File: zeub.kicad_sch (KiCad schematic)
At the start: 25 parts, among them J1 debug-port, J2 OLED-128x32, J5 Conn_01x03, J6 Conn_01x03, Q1 AO3401A, Q2 AO3401A, Q3 AO3401A, Q4 AO3401A, Q5 AO3401A, SW1 SKRHA, SW2 RotaryEncoder_Switch, U5 holyiot-18010-no-underside, U6 MT25QL128ABA1ESE

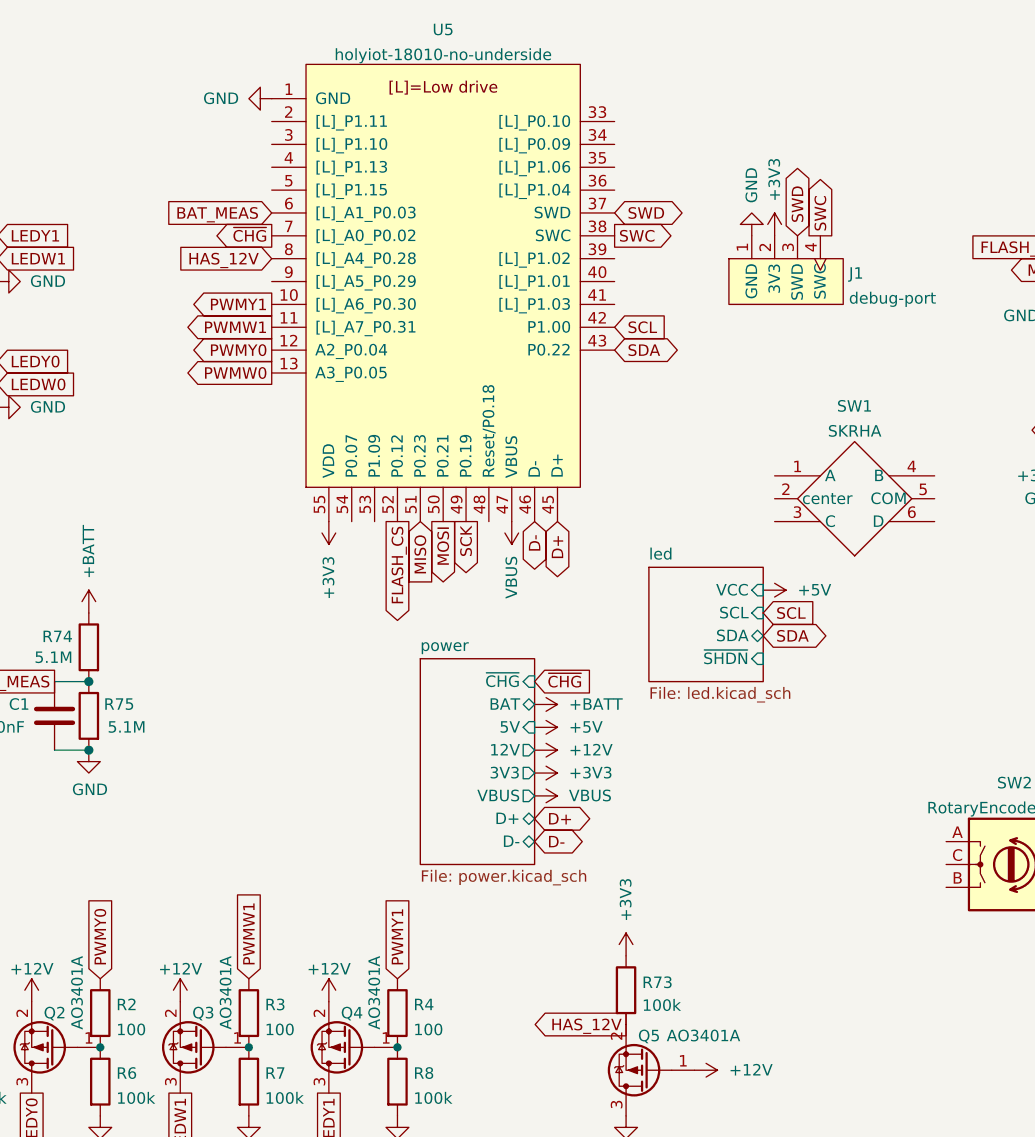
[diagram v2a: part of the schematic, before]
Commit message: routed PMU + rull RGB
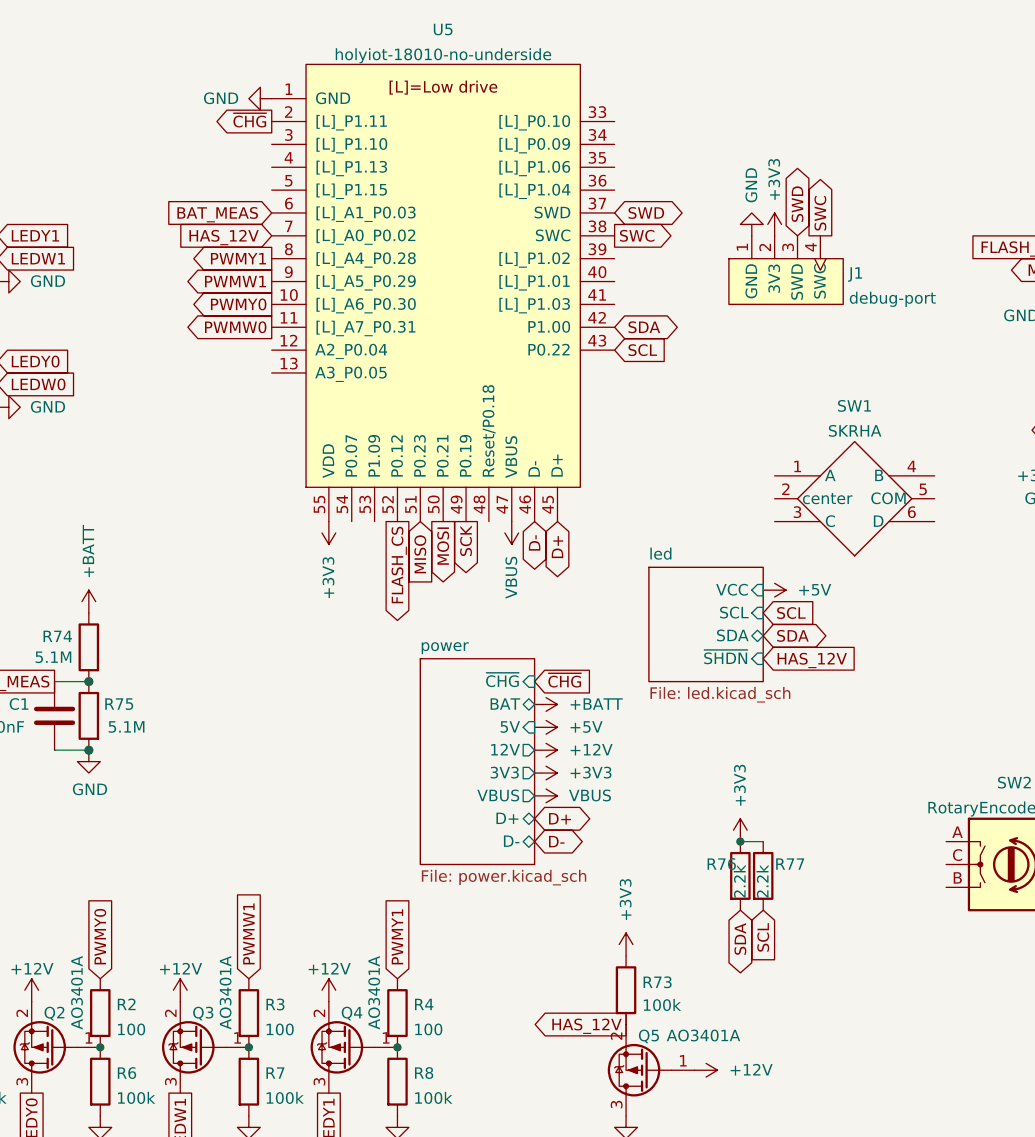
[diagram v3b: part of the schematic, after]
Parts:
- added R76, R77: 2.2k, Resistor_SMD:R_0603_1608Metric, symbol Device:R
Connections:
- net +3V3: now also R76.1, R77.1
- net HAS_12V: now also U5.7 ([L]_A0_P0.02); no longer U5.8 ([L]_A4_P0.28)
- net PWMW0: now also U5.11 ([L]_A7_P0.31); no longer U5.13 (A3_P0.05)
- net PWMW1: now also U5.9 ([L]_A5_P0.29); no longer U5.11 ([L]_A7_P0.31)
- net PWMY0: now also U5.10 ([L]_A6_P0.30); no longer U5.12 (A2_P0.04)
- net PWMY1: now also U5.8 ([L]_A4_P0.28); no longer U5.10 ([L]_A6_P0.30)
- net SCL: now also U5.43 (P0.22), R77.2; no longer U5.42 (P1.00)
- net SDA: now also U5.42 (P1.00), R76.2; no longer U5.43 (P0.22)
- net ~{CHG}: now also U5.2 ([L]_P1.11); no longer U5.7 ([L]_A0_P0.02)
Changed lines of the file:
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@@
   (junction (at 24.13 134.62) (diameter 0) (color 0 0 0 0)
+  )
+  (junction (at 111.76 111.76) (diameter 0) (color 0 0 0 0)
   )
   (junction (at 73.66 134.62) (diameter 0) (color 0 0 0 0)
@@
   (wire (pts (xy 35.56 93.98) (xy 39.37 93.98))
     (stroke (width 0) (type solid) (color 0 0 0 0))
+  )
+  (wire (pts (xy 111.76 111.76) (xy 114.3 111.76))
+    (stroke (width 0) (type default) (color 0 0 0 0))
   )
   (wire (pts (xy 39.37 101.6) (xy 35.56 101.6))
@@
     )
   )
+  (global_label "HAS_12V" (shape input) (at 114.3 91.44 0) (fields_autoplaced)
+    (effects (font (size 1.27 1.27)) (justify left))
+    (property "Intersheet References" "${INTERSHEET_REFS}" (id 0) (at 124.8169 91.5194 0)
+      (effects (font (size 1.27 1.27)) (justify left) hide)
+    )
+  )
   (global_label "SDA" (shape bidirectional) (at 114.3 88.9 0) (fields_autoplaced)
     (effects (font (size 1.27 1.27)) (justify left))
@@
     )
   )
-  (global_label "PWMW1" (shape output) (at 59.69 54.61 180) (fields_autoplaced)
+  (global_label "PWMW1" (shape output) (at 59.69 49.53 180) (fields_autoplaced)
     (effects (font (size 1.27 1.27)) (justify right))
-    (property "Intersheet References" "${INTERSHEET_REFS}" (id 0) (at 50.4431 54.6894 0)
+    (property "Intersheet References" "${INTERSHEET_REFS}" (id 0) (at 50.4431 49.6094 0)
       (effects (font (size 1.27 1.27)) (justify right) hide)
     )
@@
     )
   )
-  (global_label "PWMY1" (shape output) (at 59.69 52.07 180) (fields_autoplaced)
+  (global_label "PWMY1" (shape output) (at 59.69 46.99 180) (fields_autoplaced)
     (effects (font (size 1.27 1.27)) (justify right))
-    (property "Intersheet References" "${INTERSHEET_REFS}" (id 0) (at 50.8059 52.1494 0)
+    (property "Intersheet References" "${INTERSHEET_REFS}" (id 0) (at 50.8059 47.0694 0)
       (effects (font (size 1.27 1.27)) (justify right) hide)
     )
   )
-  (global_label "SDA" (shape bidirectional) (at 97.79 57.15 0) (fields_autoplaced)
+  (global_label "SDA" (shape bidirectional) (at 97.79 54.61 0) (fields_autoplaced)
     (effects (font (size 1.27 1.27)) (justify left))
-    (property "Intersheet References" "${INTERSHEET_REFS}" (id 0) (at 103.7712 57.0706 0)
+    (property "Intersheet References" "${INTERSHEET_REFS}" (id 0) (at 103.7712 54.6894 0)
       (effects (font (size 1.27 1.27)) (justify left) hide)
     )
@@
     )
   )
-  (global_label "PWMY0" (shape output) (at 59.69 57.15 180) (fields_autoplaced)
+  (global_label "PWMY0" (shape output) (at 59.69 52.07 180) (fields_autoplaced)
     (effects (font (size 1.27 1.27)) (justify right))
-    (property "Intersheet References" "${INTERSHEET_REFS}" (id 0) (at 50.8059 57.0706 0)
+    (property "Intersheet References" "${INTERSHEET_REFS}" (id 0) (at 50.8059 51.9906 0)
       (effects (font (size 1.27 1.27)) (justify right) hide)
     )
@@
     )
   )
-  (global_label "~{CHG}" (shape output) (at 59.69 44.45 180) (fields_autoplaced)
+  (global_label "~{CHG}" (shape output) (at 59.69 31.75 180) (fields_autoplaced)
     (effects (font (size 1.27 1.27)) (justify right))
-    (property "Intersheet References" "${INTERSHEET_REFS}" (id 0) (at 53.4064 44.3706 0)
+    (property "Intersheet References" "${INTERSHEET_REFS}" (id 0) (at 53.4064 31.6706 0)
       (effects (font (size 1.27 1.27)) (justify right) hide)
     )
@@
     )
   )
-  (global_label "PWMW0" (shape output) (at 59.69 59.69 180) (fields_autoplaced)
+  (global_label "SDA" (shape bidirectional) (at 111.76 119.38 270) (fields_autoplaced)
     (effects (font (size 1.27 1.27)) (justify right))
-    (property "Intersheet References" "${INTERSHEET_REFS}" (id 0) (at 50.4431 59.7694 0)
+    (property "Intersheet References" "${INTERSHEET_REFS}" (id 0) (at 111.8394 125.3612 90)
+      (effects (font (size 1.27 1.27)) (justify right) hide)
+    )
+  )
+  (global_label "PWMW0" (shape output) (at 59.69 54.61 180) (fields_autoplaced)
+    (effects (font (size 1.27 1.27)) (justify right))
+    (property "Intersheet References" "${INTERSHEET_REFS}" (id 0) (at 50.4431 54.6894 0)
       (effects (font (size 1.27 1.27)) (justify right) hide)
     )
@@
     )
   )
-  (global_label "SCL" (shape input) (at 97.79 54.61 0) (fields_autoplaced)
+  (global_label "SCL" (shape input) (at 97.79 57.15 0) (fields_autoplaced)
     (effects (font (size 1.27 1.27)) (justify left))
-    (property "Intersheet References" "${INTERSHEET_REFS}" (id 0) (at 103.7107 54.5306 0)
+    (property "Intersheet References" "${INTERSHEET_REFS}" (id 0) (at 103.7107 57.2294 0)
       (effects (font (size 1.27 1.27)) (justify left) hide)
     )
@@
     )
   )
+  (global_label "SCL" (shape input) (at 114.3 119.38 270) (fields_autoplaced)
+    (effects (font (size 1.27 1.27)) (justify right))
+    (property "Intersheet References" "${INTERSHEET_REFS}" (id 0) (at 114.3794 125.3007 90)
+      (effects (font (size 1.27 1.27)) (justify right) hide)
+    )
+  )
   (global_label "SWD" (shape bidirectional) (at 118.11 44.45 90) (fields_autoplaced)
     (effects (font (size 1.27 1.27)) (justify left))
@@
     )
   )
-  (global_label "HAS_12V" (shape input) (at 59.69 46.99 180) (fields_autoplaced)
+  (global_label "HAS_12V" (shape input) (at 59.69 44.45 180) (fields_autoplaced)
     (effects (font (size 1.27 1.27)) (justify right))
-    (property "Intersheet References" "${INTERSHEET_REFS}" (id 0) (at 49.1731 46.9106 0)
+    (property "Intersheet References" "${INTERSHEET_REFS}" (id 0) (at 49.1731 44.3706 0)
       (effects (font (size 1.27 1.27)) (justify right) hide)
     )
@@
     )
     (property "Datasheet" "~" (id 3) (at 57.15 138.43 0)
+      (effects (font (size 1.27 1.27)) hide)
+    )
+    (pin "1")
+    (pin "2")
+  )
+  (symbol (lib_id "Device:R") (at 114.3 115.57 0) (unit 1)
+    (in_bom yes) (on_board yes)
+    (property "Reference" "R77" (id 0) (at 115.57 114.3 0)
+      (effects (font (size 1.27 1.27)) (justify left))
+    )
+    (property "Value" "2.2k" (id 1) (at 114.3 118.11 90)
+      (effects (font (size 1.27 1.27)) (justify left))
+    )
+    (property "Footprint" "Resistor_SMD:R_0603_1608Metric" (id 2) (at 112.522 115.57 90)
+      (effects (font (size 1.27 1.27)) hide)
+    )
+    (property "Datasheet" "~" (id 3) (at 114.3 115.57 0)
       (effects (font (size 1.27 1.27)) hide)
     )
@@
     (pin "1")
   )
+  (symbol (lib_id "power:+3V3") (at 111.76 111.76 0) (unit 1)
+    (in_bom yes) (on_board yes)
+    (property "Reference" "#PWR015" (id 0) (at 111.76 115.57 0)
+      (effects (font (size 1.27 1.27)) hide)
+    )
+    (property "Value" "+3V3" (id 1) (at 111.76 107.95 90)
+      (effects (font (size 1.27 1.27)) (justify left))
+    )
+    (property "Footprint" "" (id 2) (at 111.76 111.76 0)
+      (effects (font (size 1.27 1.27)) hide)
+    )
+    (property "Datasheet" "" (id 3) (at 111.76 111.76 0)
+      (effects (font (size 1.27 1.27)) hide)
+    )
+    (pin "1")
+  )
   (symbol (lib_id "Connector_Generic:Conn_01x03") (at 24.13 46.99 180) (unit 1)
     (in_bom yes) (on_board yes) (fields_autoplaced)
@@
     (pin "1")
   )
+  (symbol (lib_id "Device:R") (at 111.76 115.57 0) (unit 1)
+    (in_bom yes) (on_board yes)
+    (property "Reference" "R76" (id 0) (at 107.95 114.3 0)
+      (effects (font (size 1.27 1.27)) (justify left))
+    )
+    (property "Value" "2.2k" (id 1) (at 111.76 118.11 90)
+      (effects (font (size 1.27 1.27)) (justify left))
+    )
+    (property "Footprint" "Resistor_SMD:R_0603_1608Metric" (id 2) (at 109.982 115.57 90)
+      (effects (font (size 1.27 1.27)) hide)
+    )
+    (property "Datasheet" "~" (id 3) (at 111.76 115.57 0)
+      (effects (font (size 1.27 1.27)) hide)
+    )
+    (pin "1")
+    (pin "2")
+  )
   (symbol (lib_id "Device:R") (at 73.66 130.81 0) (unit 1)
     (in_bom yes) (on_board yes) (fields_autoplaced)
@@
       (reference "#PWR014") (unit 1) (value "VBUS") (footprint "")
     )
+    (path "/e51724cf-48c9-47f2-ab24-c07e49a056f7"
+      (reference "#PWR015") (unit 1) (value "+3V3") (footprint "")
+    )
     (path "/321794ea-5b54-45b4-9bfc-73a794b06bcd"
       (reference "#PWR016") (unit 1) (value "+BATT") (footprint "")
@@
       (reference "R75") (unit 1) (value "5.1M") (footprint "Resistor_SMD:R_0603_1608Metric")
     )
+    (path "/f7939190-75be-4b9e-af89-0bc4e5685ada"
+      (reference "R76") (unit 1) (value "2.2k") (footprint "Resistor_SMD:R_0603_1608Metric")
+    )
+    (path "/b413a2e9-a280-422b-8e6e-7304a8d8ad3b"
+      (reference "R77") (unit 1) (value "2.2k") (footprint "Resistor_SMD:R_0603_1608Metric")
+    )
     (path "/b04ad137-4b81-4bdf-94af-319b3cefe1a6"
       (reference "SW1") (unit 1) (value "SKRHA") (footprint "switch:SKRHA-boss")
@@
     )
     (path "/0471f725-0238-4fe5-929e-b81775548504/006f97bb-ed61-44c3-b547-0190a4d34a6b"
-      (reference "U1") (unit 1) (value "IS31FL3729") (footprint "Package_DFN_QFN:QFN-32-1EP_4x4mm_P0.4mm_EP2.9x2.9mm")
+      (reference "U1") (unit 1) (value "IS31FL3729") (footprint "misc:eTQFP-32_7x7mm_P0.8mm")
     )
     (path "/0471f725-0238-4fe5-929e-b81775548504/58697035-c2a5-4a72-aa6c-0845690bbd5f"
-      (reference "U2") (unit 1) (value "IS31FL3729") (footprint "Package_DFN_QFN:QFN-32-1EP_4x4mm_P0.4mm_EP2.9x2.9mm")
+      (reference "U2") (unit 1) (value "IS31FL3729") (footprint "misc:eTQFP-32_7x7mm_P0.8mm")
     )
     (path "/0471f725-0238-4fe5-929e-b81775548504/f27e25ab-142f-46a2-b367-83f442d95b53"
-      (reference "U3") (unit 1) (value "IS31FL3729") (footprint "Package_DFN_QFN:QFN-32-1EP_4x4mm_P0.4mm_EP2.9x2.9mm")
+      (reference "U3") (unit 1) (value "IS31FL3729") (footprint "misc:eTQFP-32_7x7mm_P0.8mm")
     )
     (path "/0471f725-0238-4fe5-929e-b81775548504/487deecc-138a-43ee-8db9-7a1949bae40e"
-      (reference "U4") (unit 1) (value "IS31FL3729") (footprint "Package_DFN_QFN:QFN-32-1EP_4x4mm_P0.4mm_EP2.9x2.9mm")
+      (reference "U4") (unit 1) (value "IS31FL3729") (footprint "misc:eTQFP-32_7x7mm_P0.8mm")
     )
     (path "/be879e33-9ddf-47f3-8344-bd0208343ca1"
